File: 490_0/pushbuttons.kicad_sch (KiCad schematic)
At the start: 29 parts, among them J1 B2B-XH-A, J15 B2B-XH-A, J17 B2B-XH-A, J18 B2B-XH-A, J19 B2B-XH-A, J2 B2B-XH-A, SW4 SW_Push0, SW5 SW_Push0, SW6 SW_Push0, SW7 SW_Push0, SW8 SW_Push0

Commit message: changed PCB block diagram
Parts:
- removed J1, J15, J17, J18, J19, J2: B2B-XH-A, B2B-XH-A:JST_B2B-XH-A, symbol capstone_parts:B2B-XH-A
- added J1, J6: Conn_01x08, 4ms_Connector:Pins_1x08_2.54mm_TH, symbol PCM_4ms_Connector:Conn_01x08
- added SW9: SW_Push0, symbol Switch:SW_Push
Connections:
- net +3.3V: now also J6.7 (Pin_7); no longer R38.2, R39.2, R40.2, R41.2, R42.2, R53.2
- net GND: now also SW4.1, SW5.1, SW6.1, SW7.1, SW8.1, J1.8 (Pin_8), J6.8 (Pin_8), SW9.1
- net GPIO10: now also J6.5 (Pin_5); no longer C54.1 (+), R46.2
- net GPIO17: now also J6.1 (Pin_1); no longer C16.1 (+), R54.2
- net GPIO22: now also J6.2 (Pin_2); no longer C51.1 (+), R43.2
- net GPIO23: now also J6.3 (Pin_3); no longer C52.1 (+), R44.2
- net GPIO24: now also J6.4 (Pin_4); no longer C53.1 (+), R45.2
- net GPIO25: now also J6.6 (Pin_6); no longer C55.1 (+), R47.2
- net at R42.1, R47.1: now also SW9.2
- net at R39.1, R44.1: now also SW6.2
- net at R40.1, R45.1: now also SW7.2
- net at R38.1, R43.1: now also SW5.2
- net at R53.1, R54.1: now also SW4.2
- net at R41.1, R46.1: now also SW8.2
- new net Button_1: C16.1 (+), J1.1 (Pin_1), R54.2
- new net Button_2: C51.1 (+), J1.2 (Pin_2), R43.2
- new net Button_3: C52.1 (+), J1.3 (Pin_3), R44.2
- new net Button_4: C53.1 (+), J1.4 (Pin_4), R45.2
- new net Button_5: C54.1 (+), J1.5 (Pin_5), R46.2
- new net Button_6: C55.1 (+), J1.6 (Pin_6), R47.2
- new net VBUTTON: J1.7 (Pin_7), R38.2, R39.2, R40.2, R41.2, R42.2, R53.2
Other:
- note removed: "To Turn ON: When the Pi is OFF/halted - shorting GPIO3 to Ground wakes it up. To Turn OFF: When the Pi is ON - run a script that listens for a button press on GPIO3 and issues the command sudo shutdown -h now"
- moved on the sheet: SW4, SW5, SW6, SW7, SW8

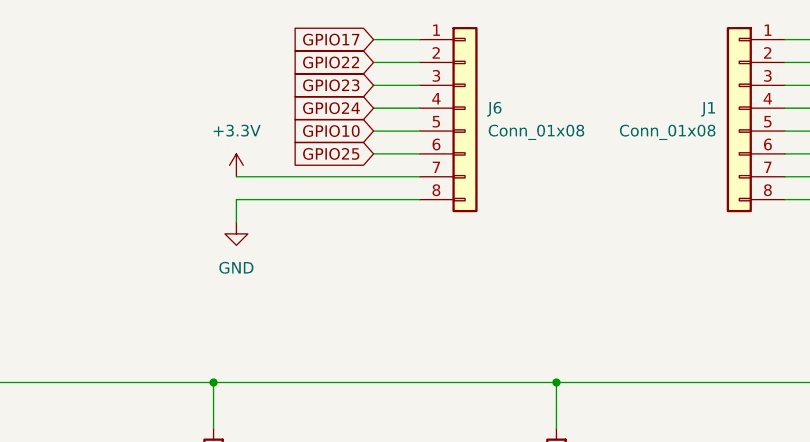
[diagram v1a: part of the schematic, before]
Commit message: Changed PCB block dagram and layout
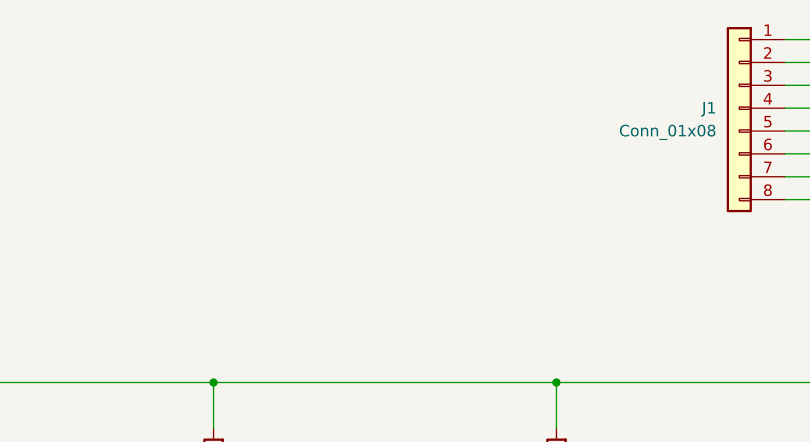
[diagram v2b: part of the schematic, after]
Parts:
- removed J6: Conn_01x08, 4ms_Connector:Pins_1x08_2.54mm_TH, symbol PCM_4ms_Connector:Conn_01x08

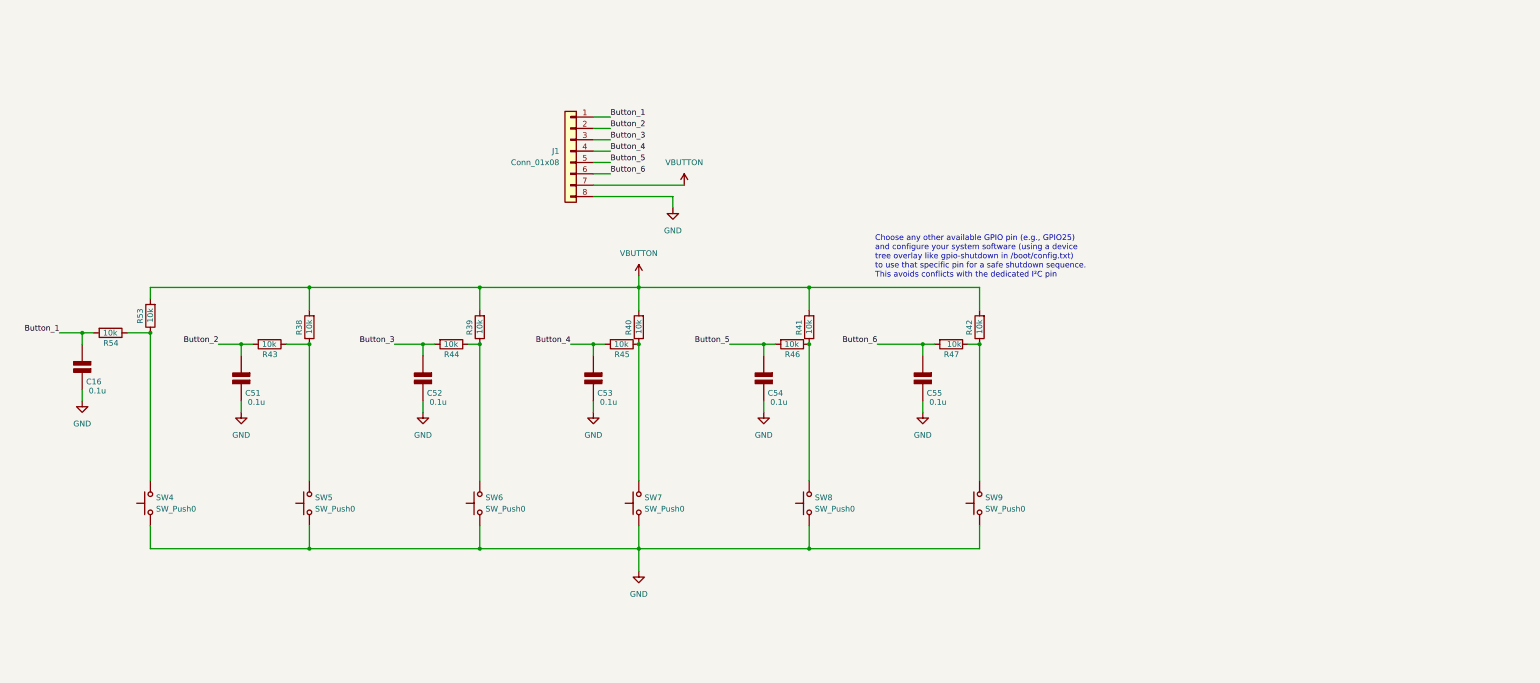
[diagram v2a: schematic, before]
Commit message: Schematic layout update
- applied hierarchical labels
- cleaned up the schematic
- finalized CM4 connections
- checked cm4 connections
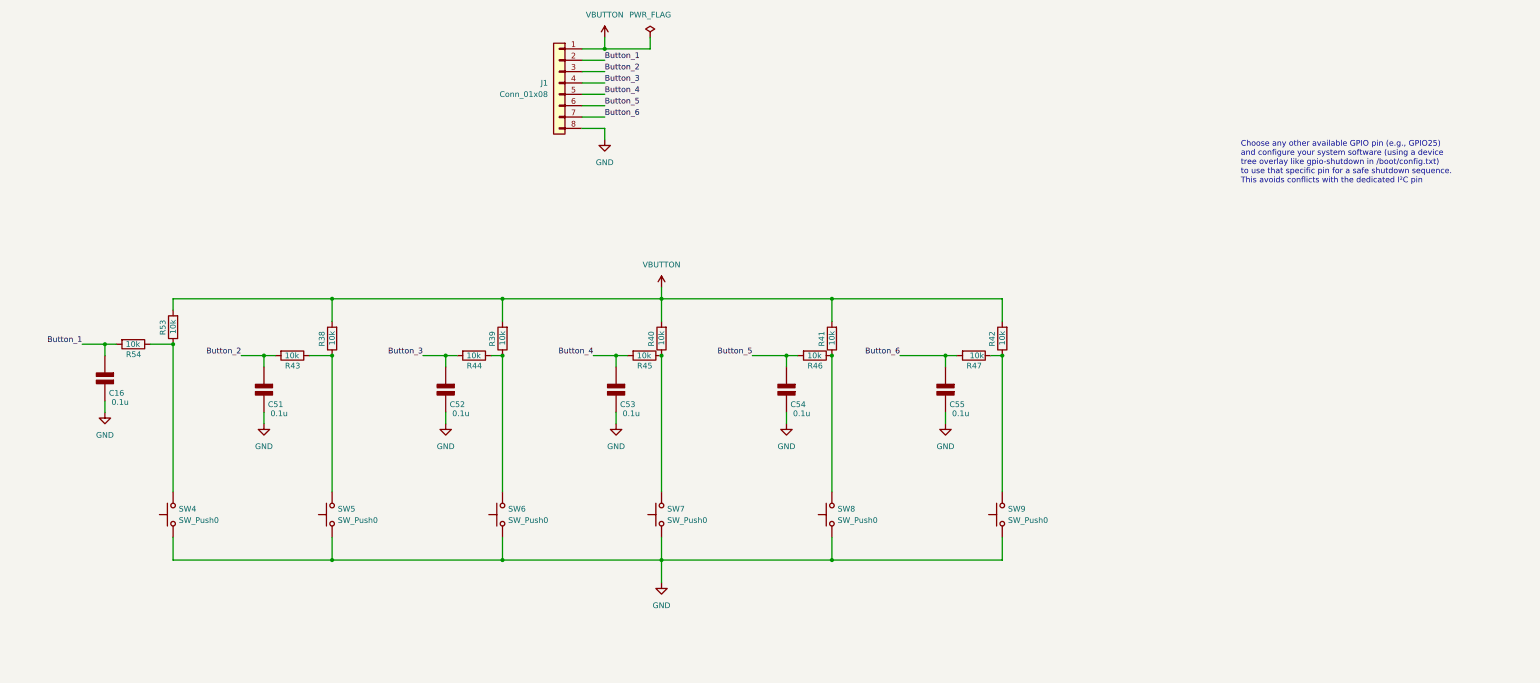
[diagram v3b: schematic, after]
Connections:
- net Button_1: now also J1.2 (Pin_2); no longer J1.1 (Pin_1)
- net Button_2: now also J1.3 (Pin_3); no longer J1.2 (Pin_2)
- net Button_3: now also J1.4 (Pin_4); no longer J1.3 (Pin_3)
- net Button_4: now also J1.5 (Pin_5); no longer J1.4 (Pin_4)
- net Button_5: now also J1.6 (Pin_6); no longer J1.5 (Pin_5)
- net Button_6: now also J1.7 (Pin_7); no longer J1.6 (Pin_6)
- net VBUTTON: now also J1.1 (Pin_1); no longer J1.7 (Pin_7)
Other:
- moved on the sheet: C16, C51, C52, C53, C54, C55, J1, R38, R39, R40, R41, R42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

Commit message: Power + BOM update
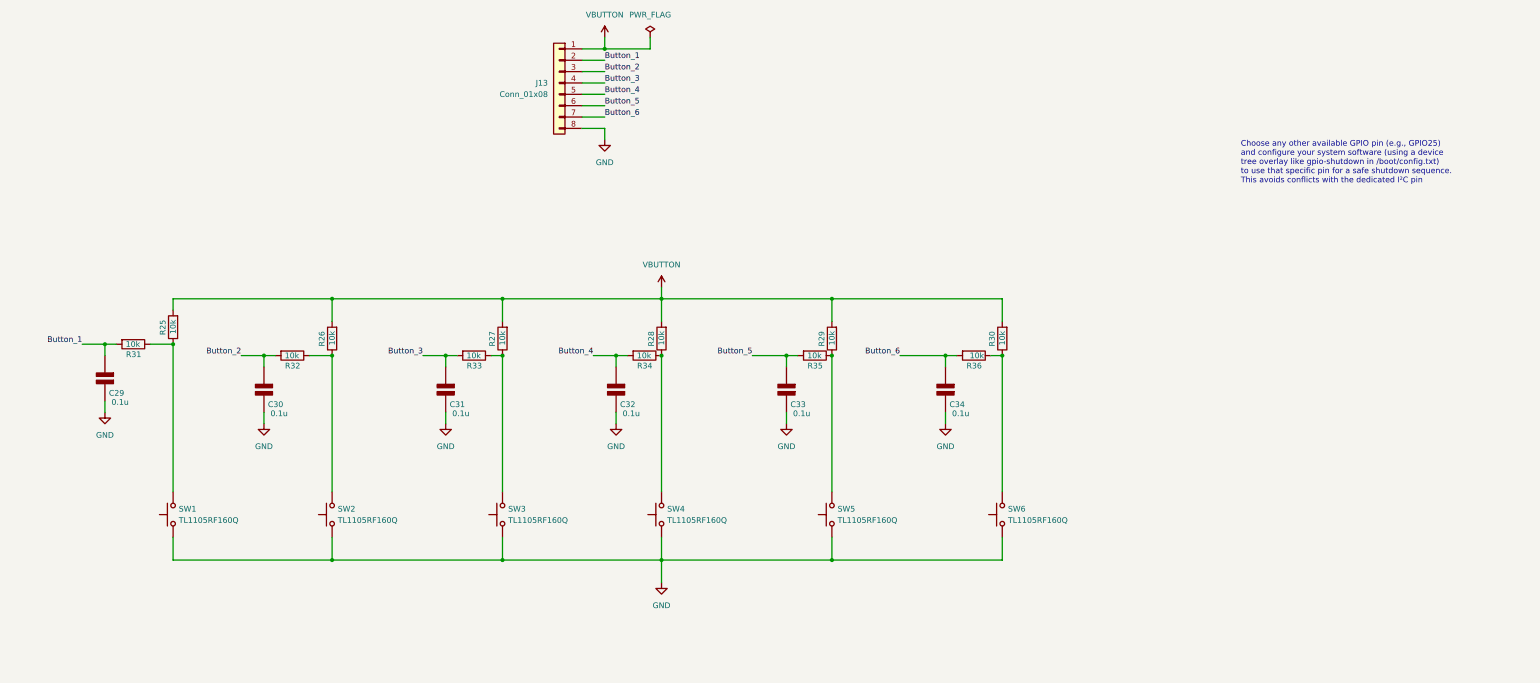
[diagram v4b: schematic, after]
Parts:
- J13: renamed from J1; footprint 4ms_Connector:Pins_1x08_2.54mm_TH -> (none)
- SW1: renamed from SW4; value SW_Push0 -> TL1105RF160Q; Digikey Link (none) -> https://www.digikey.ca/en/products/detail/e-switch/TL1105RF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; Manufacturer (none) -> E-Switch; Manufacturer Part (none) -> TL1105RF160Q; Price (none) -> 0.37; Supplier (none) -> DigiKey; Supplier P/N (none) -> EG1837-ND; Type (none) -> Through Hole, Right Angle; Unit (none) -> pcs
- SW2: renamed from SW5; value SW_Push0 -> TL1105RF160Q; Digikey Link (none) -> https://www.digikey.ca/en/products/detail/e-switch/TL1105RF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; Manufacturer (none) -> E-Switch; Manufacturer Part (none) -> TL1105RF160Q; Price (none) -> 0.37; Supplier (none) -> DigiKey; Supplier P/N (none) -> EG1837-ND; Type (none) -> Through Hole, Right Angle; Unit (none) -> pcs
- SW3: renamed from SW6; value SW_Push0 -> TL1105RF160Q; Digikey Link (none) -> https://www.digikey.ca/en/products/detail/e-switch/TL1105RF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; Manufacturer (none) -> E-Switch; Manufacturer Part (none) -> TL1105RF160Q; Price (none) -> 0.37; Supplier (none) -> DigiKey; Supplier P/N (none) -> EG1837-ND; Type (none) -> Through Hole, Right Angle; Unit (none) -> pcs
- SW4: renamed from SW7; value SW_Push0 -> TL1105RF160Q; Digikey Link (none) -> https://www.digikey.ca/en/products/detail/e-switch/TL1105RF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; Manufacturer (none) -> E-Switch; Manufacturer Part (none) -> TL1105RF160Q; Price (none) -> 0.37; Supplier (none) -> DigiKey; Supplier P/N (none) -> EG1837-ND; Type (none) -> Through Hole, Right Angle; Unit (none) -> pcs
- SW5: renamed from SW8; value SW_Push0 -> TL1105RF160Q; Digikey Link (none) -> https://www.digikey.ca/en/products/detail/e-switch/TL1105RF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; Manufacturer (none) -> E-Switch; Manufacturer Part (none) -> TL1105RF160Q; Price (none) -> 0.37; Supplier (none) -> DigiKey; Supplier P/N (none) -> EG1837-ND; Type (none) -> Through Hole, Right Angle; Unit (none) -> pcs
- SW6: renamed from SW9; value SW_Push0 -> TL1105RF160Q; Digikey Link (none) -> https://www.digikey.ca/en/products/detail/e-switch/TL1105RF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; Manufacturer (none) -> E-Switch; Manufacturer Part (none) -> TL1105RF160Q; Price (none) -> 0.37; Supplier (none) -> DigiKey; Supplier P/N (none) -> EG1837-ND; Type (none) -> Through Hole, Right Angle; Unit (none) -> pcs
- renumbered C16 to C29, C51 to C30, C52 to C31, C53 to C32, C54 to C33, C55 to C34, R53 to R25, R38 to R26, R39 to R27, R40 to R28, R41 to R29, R42 to R30, R54 to R31, R43 to R32, R44 to R33, R45 to R34, R46 to R35, R47 to R36

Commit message: finished BOM
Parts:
- C29, C30, C31, C32, C33, C34: Digikey Link (none) -> https://www.digikey.ca/en/products/detail/samsung-electro-m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; Manufacturer (none) -> Samsung Electro-Mechanics; Manufacturer Part (none) -> CL31B104KBCNNNC; Package (none) -> 1206 (3216 Metric); Price (none) -> 0.11; Supplier (none) -> DigiKey; Supplier P/N (none) -> 1276-1017-1-ND; Type (none) -> SMD, MLCC; Unit (none) -> pcs
- J13: Digikey Link (none) -> https://www.digikey.ca/en/products/detail/jst-sales-america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; Manufacturer (none) -> JST Sales America Inc.; Manufacturer Part (none) -> S8B-XH-A; Price (none) -> 0.33; Supplier (none) -> DigiKey; Supplier P/N (none) -> 455-S8B-XH-A-ND; Type (none) -> Through Hole; Unit (none) -> pcs
- R25, R26, R27, R28, R29, R30, R31, R32, R33, R34, R35, R36: Digikey Link (none) -> https://www.digikey.ca/en/products/detail/yageo/RC1206FR-07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; Manufacturer (none) -> YAGEO; Manufacturer Part (none) -> RC1206FR-0710KL; Package (none) -> 1206; Price (none) -> 0.1; Supplier (none) -> DigiKey; Supplier P/N (none) -> 311-10.0KFRCT-ND; Type (none) -> SMD; Unit (none) -> pcs

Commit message: Updated the schematic
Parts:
- removed J13: Conn_01x08, symbol PCM_4ms_Connector:Conn_01x08
- renumbered C29 to C37, C30 to C38, C31 to C39, C32 to C40, C33 to C41, C34 to C42, R25 to R1, R26 to R2, R27 to R39, R28 to R40, R29 to R41, R30 to R42, R31 to R56, R32 to R58, R33 to R59, R34 to R60, R35 to R63, R36 to R64, SW3 to SW10, SW4 to SW11, SW5 to SW12, SW6 to SW13, SW1 to SW7, SW2 to SW8
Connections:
- net Button_1 renamed GPIO22
- net Button_2 renamed GPIO23
- net Button_3 renamed GPIO24
- net Button_4 renamed GPIO25
- net Button_5 renamed GPIO10
- net Button_6 renamed GPIO17
- net VBUTTON renamed +3.3V

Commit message: Implemented Dmitry comments
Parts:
- SW1: renamed from SW7; value TL1105RF160Q -> TL1105LF160Q; Digikey Link https://www.digikey.ca/en/products/detail/e-switch/TL1105RF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 -> https://www.digikey.ca/en/products/detail/e-switch/tl1105lf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; Manufacturer Part TL1105RF160Q -> TL1105LF160Q; Price 0.37 -> 0.33; Supplier P/N EG1837-ND -> EG2505-ND
- SW2: renamed from SW8; value TL1105RF160Q -> TL1105LF160Q; Digikey Link https://www.digikey.ca/en/products/detail/e-switch/TL1105RF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 -> https://www.digikey.ca/en/products/detail/e-switch/tl1105lf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; Manufacturer Part TL1105RF160Q -> TL1105LF160Q; Price 0.37 -> 0.33; Supplier P/N EG1837-ND -> EG2505-ND
- SW3: renamed from SW10; value TL1105RF160Q -> TL1105LF160Q; Digikey Link https://www.digikey.ca/en/products/detail/e-switch/TL1105RF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 -> https://www.digikey.ca/en/products/detail/e-switch/tl1105lf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; Manufacturer Part TL1105RF160Q -> TL1105LF160Q; Price 0.37 -> 0.33; Supplier P/N EG1837-ND -> EG2505-ND
- SW4: renamed from SW11; value TL1105RF160Q -> TL1105LF160Q; Digikey Link https://www.digikey.ca/en/products/detail/e-switch/TL1105RF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 -> https://www.digikey.ca/en/products/detail/e-switch/tl1105lf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; Manufacturer Part TL1105RF160Q -> TL1105LF160Q; Price 0.37 -> 0.33; Supplier P/N EG1837-ND -> EG2505-ND
- SW5: renamed from SW12; value TL1105RF160Q -> TL1105LF160Q; Digikey Link https://www.digikey.ca/en/products/detail/e-switch/TL1105RF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 -> https://www.digikey.ca/en/products/detail/e-switch/tl1105lf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; Manufacturer Part TL1105RF160Q -> TL1105LF160Q; Price 0.37 -> 0.33; Supplier P/N EG1837-ND -> EG2505-ND
- SW6: renamed from SW13; value TL1105RF160Q -> TL1105LF160Q; Digikey Link https://www.digikey.ca/en/products/detail/e-switch/TL1105RF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 -> https://www.digikey.ca/en/products/detail/e-switch/tl1105lf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; Manufacturer Part TL1105RF160Q -> TL1105LF160Q; Price 0.37 -> 0.33; Supplier P/N EG1837-ND -> EG2505-ND
- renumbered C37 to C3, C38 to C4, C39 to C5, C40 to C6, C41 to C7, C42 to C8, R58 to R10, R59 to R11, R60 to R12, R63 to R13, R64 to R14, R1 to R3, R2 to R4, R39 to R5, R40 to R6, R41 to R7, R42 to R8, R56 to R9
